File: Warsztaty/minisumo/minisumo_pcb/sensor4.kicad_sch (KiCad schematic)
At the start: 1 part

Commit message: chyba gotowy schemat
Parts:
- removed SPI1: MTSW-103-23-F-D-230, MTSW-103-23-F-D-230:SAMTEC_MTSW-103-23-F-D-230, symbol MTSW-103-23-F-D-230:MTSW-103-23-F-D-230
- added SPI5: MTSW-103-23-F-D-230, MTSW-103-23-F-D-230:SAMTEC_MTSW-103-23-F-D-230, symbol MTSW-103-23-F-D-230:MTSW-103-23-F-D-230
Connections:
- net +5V: now also SPI5.02
- net GND: now also SPI5.01
- new net G4: SPI5.06
- new net SCL: SPI5.04
- new net SDA: SPI5.03
- new net X4: SPI5.05
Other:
- note added: "Sensor4"
- note removed: "Programming connector"
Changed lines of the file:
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@@
 	(wire
 		(pts
-			(xy 62.23 35.56) (xy 62.23 39.37)
-		)
-		(stroke
-			(width 0)
-			(type default)
-		)
-	)
-	(wire
-		(pts
-			(xy 59.69 35.56) (xy 62.23 35.56)
+			(xy 24.13 30.48) (xy 34.29 30.48)
+		)
+		(stroke
+			(width 0)
+			(type default)
+		)
+	)
+	(wire
+		(pts
+			(xy 59.69 30.48) (xy 62.23 30.48)
+		)
+		(stroke
+			(width 0)
+			(type default)
+		)
+	)
+	(wire
+		(pts
+			(xy 24.13 38.1) (xy 24.13 30.48)
+		)
+		(stroke
+			(width 0)
+			(type default)
+		)
+	)
+	(wire
+		(pts
+			(xy 59.69 35.56) (xy 60.96 35.56)
+		)
+		(stroke
+			(width 0)
+			(type default)
+		)
+	)
+	(wire
+		(pts
+			(xy 59.69 33.02) (xy 60.96 33.02)
+		)
+		(stroke
+			(width 0)
+			(type default)
+		)
+	)
+	(wire
+		(pts
+			(xy 33.02 33.02) (xy 34.29 33.02)
 		)
 		(stroke
@@
 		(pts
 			(xy 62.23 29.21) (xy 62.23 30.48)
-		)
-		(stroke
-			(width 0)
-			(type default)
-		)
-	)
-	(wire
-		(pts
-			(xy 33.02 33.02) (xy 34.29 33.02)
-		)
-		(stroke
-			(width 0)
-			(type default)
-		)
-	)
-	(wire
-		(pts
-			(xy 59.69 30.48) (xy 62.23 30.48)
-		)
-		(stroke
-			(width 0)
-			(type default)
-		)
-	)
-	(wire
-		(pts
-			(xy 59.69 33.02) (xy 60.96 33.02)
 		)
 		(stroke
@@
 		)
 	)
-	(text "Programming connector"
+	(text "Sensor4\n"
 		(exclude_from_sim no)
 		(at 27.686 16.256 0)
@@
 		)
 	)
-	(hierarchical_label "SCK"
+	(hierarchical_label "X4"
 		(shape input)
-		(at 33.02 33.02 180)
+		(at 33.02 35.56 180)
 		(fields_autoplaced yes)
 		(effects
@@
 		)
 	)
-	(hierarchical_label "RST"
+	(hierarchical_label "G4"
 		(shape input)
-		(at 33.02 35.56 180)
+		(at 60.96 35.56 0)
 		(fields_autoplaced yes)
 		(effects
@@
 				(size 0.762 0.762)
 			)
-			(justify right)
-		)
-	)
-	(hierarchical_label "MOSI"
+			(justify left)
+		)
+	)
+	(hierarchical_label "SCL"
 		(shape input)
 		(at 60.96 33.02 0)
@@
 		)
 	)
-	(hierarchical_label "MISO"
+	(hierarchical_label "SDA"
 		(shape input)
-		(at 34.29 30.48 180)
+		(at 33.02 33.02 180)
 		(fields_autoplaced yes)
 		(effects
@@
 			)
 			(justify right)
+		)
+	)
+	(symbol
+		(lib_id "power:GND")
+		(at 24.13 38.1 0)
+		(unit 1)
+		(exclude_from_sim no)
+		(in_bom yes)
+		(on_board yes)
+		(dnp no)
+		(fields_autoplaced yes)
+		(property "Reference" "#PWR025"
+			(at 24.13 44.45 0)
+			(effects
+				(font
+					(size 1.27 1.27)
+				)
+				(hide yes)
+			)
+		)
+		(property "Value" "GND"
+			(at 24.13 43.18 0)
+			(effects
+				(font
+					(size 1.27 1.27)
+				)
+			)
+		)
+		(property "Footprint" ""
+			(at 24.13 38.1 0)
+			(effects
+				(font
+					(size 1.27 1.27)
+				)
+				(hide yes)
+			)
+		)
+		(property "Datasheet" ""
+			(at 24.13 38.1 0)
+			(effects
+				(font
+					(size 1.27 1.27)
+				)
+				(hide yes)
+			)
+		)
+		(property "Description" "Power symbol creates a global label with name \"GND\" , ground"
+			(at 24.13 38.1 0)
+			(effects
+				(font
+					(size 1.27 1.27)
+				)
+				(hide yes)
+			)
+		)
+		(pin "1"
+		)
+		(instances
+			(project "minisumo_pcb"
+				(path "/7b99a4ad-c15f-48f5-acdf-b2b295c8ee3b/fd8559db-718b-46e4-b9e8-fb43a36357b7"
+					(reference "#PWR025")
+					(unit 1)
+				)
+			)
+		)
+	)
+	(symbol
+		(lib_id "power:+5V")
+		(at 62.23 29.21 0)
+		(unit 1)
+		(exclude_from_sim no)
+		(in_bom yes)
+		(on_board yes)
+		(dnp no)
+		(fields_autoplaced yes)
+		(property "Reference" "#PWR028"
+			(at 62.23 33.02 0)
+			(effects
+				(font
+					(size 1.27 1.27)
+				)
+				(hide yes)
+			)
+		)
+		(property "Value" "+5V"
+			(at 62.23 24.13 0)
+			(effects
+				(font
+					(size 1.27 1.27)
+				)
+			)
+		)
+		(property "Footprint" ""
+			(at 62.23 29.21 0)
+			(effects
+				(font
+					(size 1.27 1.27)
+				)
+				(hide yes)
+			)
+		)
+		(property "Datasheet" ""
+			(at 62.23 29.21 0)
+			(effects
+				(font
+					(size 1.27 1.27)
+				)
+				(hide yes)
+			)
+		)
+		(property "Description" "Power symbol creates a global label with name \"+5V\""
+			(at 62.23 29.21 0)
+			(effects
+				(font
+					(size 1.27 1.27)
+				)
+				(hide yes)
+			)
+		)
+		(pin "1"
+		)
+		(instances
+			(project "minisumo_pcb"
+				(path "/7b99a4ad-c15f-48f5-acdf-b2b295c8ee3b/fd8559db-718b-46e4-b9e8-fb43a36357b7"
+					(reference "#PWR028")
+					(unit 1)
+				)
+			)
 		)
 	)
@@
 		(on_board yes)
 		(dnp no)
-		(property "Reference" "SPI1"
+		(property "Reference" "SPI5"
 			(at 46.99 26.416 0)
 			(effects
@@
 		(instances
 			(project "minisumo_pcb"
-				(path "/7b99a4ad-c15f-48f5-acdf-b2b295c8ee3b/d44754c4-1248-482d-a92b-4192f4f09fb1"
-					(reference "SPI1")
+				(path "/7b99a4ad-c15f-48f5-acdf-b2b295c8ee3b/fd8559db-718b-46e4-b9e8-fb43a36357b7"
+					(reference "SPI5")
 					(unit 1)
 				)
-			)
-		)
-	)
-	(symbol
-		(lib_id "power:GND")
-		(at 62.23 39.37 0)
-		(unit 1)
-		(exclude_from_sim no)
-		(in_bom yes)
-		(on_board yes)
-		(dnp no)
-		(fields_autoplaced yes)
-		(property "Reference" "#PWR02"
-			(at 62.23 45.72 0)
-			(effects
-				(font
-					(size 1.27 1.27)
-				)
-				(hide yes)
-			)
-		)
-		(property "Value" "GND"
-			(at 62.23 44.45 0)
-			(effects
-				(font
-					(size 1.27 1.27)
-				)
-			)
-		)
-		(property "Footprint" ""
-			(at 62.23 39.37 0)
-			(effects
-				(font
-					(size 1.27 1.27)
-				)
-				(hide yes)
-			)
-		)
-		(property "Datasheet" ""
-			(at 62.23 39.37 0)
-			(effects
-				(font
-					(size 1.27 1.27)
-				)
-				(hide yes)
-			)
-		)
-		(property "Description" "Power symbol creates a global label with name \"GND\" , ground"
-			(at 62.23 39.37 0)
-			(effects
-				(font
-					(size 1.27 1.27)
-				)
-				(hide yes)
-			)
-		)
-		(pin "1"
-		)
-		(instances
-			(project "minisumo_pcb"
-				(path "/7b99a4ad-c15f-48f5-acdf-b2b295c8ee3b/d44754c4-1248-482d-a92b-4192f4f09fb1"
-					(reference "#PWR02")
-					(unit 1)
-				)
-			)
-		)
-	)
-	(symbol
-		(lib_id "power:+5V")
-		(at 62.23 29.21 0)
-		(unit 1)
-		(exclude_from_sim no)
-		(in_bom yes)
-		(on_board yes)
-		(dnp no)
-		(fields_autoplaced yes)
-		(property "Reference" "#PWR035"
-			(at 62.23 33.02 0)
-			(effects
-				(font
-					(size 1.27 1.27)
-				)
-				(hide yes)
-			)
-		)
-		(property "Value" "+5V"
-			(at 62.23 24.13 0)
-			(effects
-				(font
-					(size 1.27 1.27)
-				)
-			)
-		)
-		(property "Footprint" ""
-			(at 62.23 29.21 0)
-			(effects
-				(font
-					(size 1.27 1.27)
-				)
-				(hide yes)
-			)
-		)
-		(property "Datasheet" ""
-			(at 62.23 29.21 0)
-			(effects
-				(font
-					(size 1.27 1.27)
-				)
-				(hide yes)
-			)
-		)
-		(property "Description" "Power symbol creates a global label with name \"+5V\""
-			(at 62.23 29.21 0)
-			(effects
-				(font
-					(size 1.27 1.27)
-				)
-				(hide yes)
-			)
-		)
-		(pin "1"
-		)
-		(instances
-			(project "minisumo_pcb"
-				(path "/7b99a4ad-c15f-48f5-acdf-b2b295c8ee3b/d44754c4-1248-482d-a92b-4192f4f09fb1"
-					(reference "#PWR035")
-					(unit 1)
-				)

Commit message: stan przed usunięciem jednego czujnika lini
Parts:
- added R11: 20k, Resistor_SMD:R_0805_2012Metric, symbol Device:R_Small
- added R12: 10k, Resistor_SMD:R_0805_2012Metric, symbol Device:R_Small
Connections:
- net GND: now also R11.1
- net X4: now also R11.2, R12.2; no longer SPI5.05
- new net: R12.1, SPI5.05

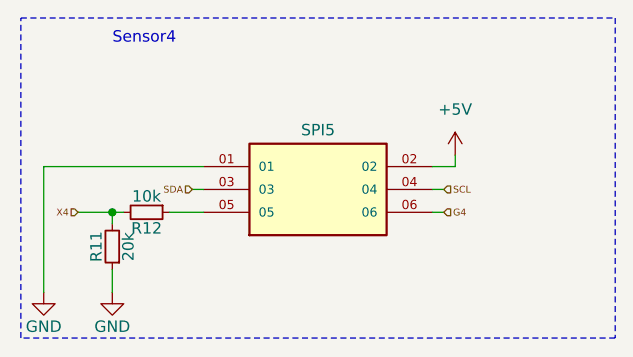
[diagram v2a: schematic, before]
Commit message: Wstępny wyglad robota i płytki
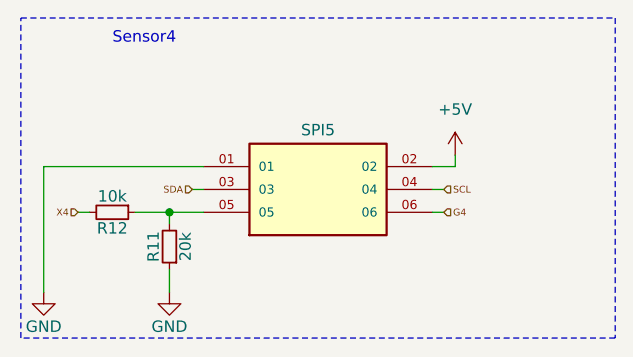
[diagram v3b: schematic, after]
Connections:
- net X4: no longer R11.2
- net at R12.1, SPI5.05: now also R11.2
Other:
- moved on the sheet: R11, R12
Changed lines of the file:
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@@
 	(paper "A4")
 	(junction
-		(at 24.13 35.56)
+		(at 30.48 35.56)
 		(diameter 0)
 		(color 0 0 0 0)
@@
 	(wire
 		(pts
-			(xy 24.13 35.56) (xy 24.13 36.83)
-		)
-		(stroke
-			(width 0)
-			(type default)
-		)
-	)
-	(wire
-		(pts
 			(xy 59.69 30.48) (xy 62.23 30.48)
 		)
@@
 	(wire
 		(pts
+			(xy 26.67 35.56) (xy 30.48 35.56)
+		)
+		(stroke
+			(width 0)
+			(type default)
+		)
+	)
+	(wire
+		(pts
+			(xy 16.51 44.45) (xy 16.51 30.48)
+		)
+		(stroke
+			(width 0)
+			(type default)
+		)
+	)
+	(wire
+		(pts
 			(xy 30.48 35.56) (xy 34.29 35.56)
 		)
@@
 	(wire
 		(pts
-			(xy 16.51 44.45) (xy 16.51 30.48)
-		)
-		(stroke
-			(width 0)
-			(type default)
-		)
-	)
-	(wire
-		(pts
-			(xy 24.13 35.56) (xy 25.4 35.56)
-		)
-		(stroke
-			(width 0)
-			(type default)
-		)
-	)
-	(wire
-		(pts
-			(xy 24.13 41.91) (xy 24.13 44.45)
+			(xy 30.48 41.91) (xy 30.48 44.45)
 		)
 		(stroke
@@
 	(wire
 		(pts
+			(xy 30.48 35.56) (xy 30.48 36.83)
+		)
+		(stroke
+			(width 0)
+			(type default)
+		)
+	)
+	(wire
+		(pts
 			(xy 59.69 33.02) (xy 60.96 33.02)
 		)
@@
 	(wire
 		(pts
-			(xy 20.32 35.56) (xy 24.13 35.56)
+			(xy 20.32 35.56) (xy 21.59 35.56)
 		)
 		(stroke
@@
 	(symbol
 		(lib_id "Device:R_Small")
-		(at 24.13 39.37 180)
+		(at 30.48 39.37 180)
 		(unit 1)
 		(exclude_from_sim no)
@@
 		(dnp no)
 		(property "Reference" "R11"
-			(at 22.352 39.37 90)
+			(at 28.702 39.37 90)
 			(effects
 				(font
@@
 		)
 		(property "Value" "20k"
-			(at 25.908 39.37 90)
+			(at 32.258 39.37 90)
 			(effects
 				(font
@@
 		)
 		(property "Footprint" "Resistor_SMD:R_0805_2012Metric"
-			(at 24.13 39.37 0)
+			(at 30.48 39.37 0)
 			(effects
 				(font
@@
 		)
 		(property "Datasheet" "~"
-			(at 24.13 39.37 0)
+			(at 30.48 39.37 0)
 			(effects
 				(font
@@
 		)
 		(property "Description" "Resistor, small symbol"
-			(at 24.13 39.37 0)
+			(at 30.48 39.37 0)
 			(effects
 				(font
@@
 	(symbol
 		(lib_id "Device:R_Small")
-		(at 27.94 35.56 270)
+		(at 24.13 35.56 270)
 		(unit 1)
 		(exclude_from_sim no)
@@
 		(dnp no)
 		(property "Reference" "R12"
-			(at 27.94 37.338 90)
+			(at 24.13 37.338 90)
 			(effects
 				(font
@@
 		)
 		(property "Value" "10k"
-			(at 27.94 33.782 90)
+			(at 24.13 33.782 90)
 			(effects
 				(font
@@
 		)
 		(property "Footprint" "Resistor_SMD:R_0805_2012Metric"
-			(at 27.94 35.56 0)
+			(at 24.13 35.56 0)
 			(effects
 				(font
@@
 		)
 		(property "Datasheet" "~"
-			(at 27.94 35.56 0)
+			(at 24.13 35.56 0)
 			(effects
 				(font
@@
 		)
 		(property "Description" "Resistor, small symbol"
-			(at 27.94 35.56 0)
+			(at 24.13 35.56 0)
 			(effects
 				(font
@@
 	(symbol
 		(lib_id "power:GND")
-		(at 24.13 44.45 0)
+		(at 30.48 44.45 0)
 		(unit 1)
 		(exclude_from_sim no)
@@
 		(dnp no)
 		(property "Reference" "#PWR032"
-			(at 24.13 50.8 0)
+			(at 30.48 50.8 0)
 			(effects
 				(font
@@
 		)
 		(property "Value" "GND"
-			(at 24.13 48.26 0)
+			(at 30.48 48.26 0)
 			(effects
 				(font
@@
 		)
 		(property "Footprint" ""
-			(at 24.13 44.45 0)
+			(at 30.48 44.45 0)
 			(effects
 				(font
@@
 		)
 		(property "Datasheet" ""
-			(at 24.13 44.45 0)
+			(at 30.48 44.45 0)
 			(effects
 				(font
@@
 		)
 		(property "Description" "Power symbol creates a global label with name \"GND\" , ground"
-			(at 24.13 44.45 0)
-			(effects
-				(font
+			(at 30.48 44.45 0)
+			(effects
+				(font

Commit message: koncowy projekt plytki i chyba model tez
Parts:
- renumbered SPI5 to ES4
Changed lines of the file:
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@@
 		(on_board yes)
 		(dnp no)
-		(property "Reference" "SPI5"
+		(property "Reference" "ES4"
 			(at 46.99 26.416 0)
 			(effects
@@
 			(project "minisumo_pcb"
 				(path "/7b99a4ad-c15f-48f5-acdf-b2b295c8ee3b/fd8559db-718b-46e4-b9e8-fb43a36357b7"
-					(reference "SPI5")
+					(reference "ES4")
 					(unit 1)
 				)

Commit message: prawdopodobnie koncowa wersja płytki
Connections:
- net X4 renamed XSHUT_4
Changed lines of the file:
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@@
 		)
 	)
-	(hierarchical_label "X4"
+	(hierarchical_label "XSHUT_4"
 		(shape input)
 		(at 20.32 35.56 180)
